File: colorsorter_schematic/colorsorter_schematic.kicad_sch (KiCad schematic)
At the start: 35 parts, among them SW2 SW_SPDT, U1 PIC24FJ64GA702-I/SO, U2 ESP8266-01_ESP-01

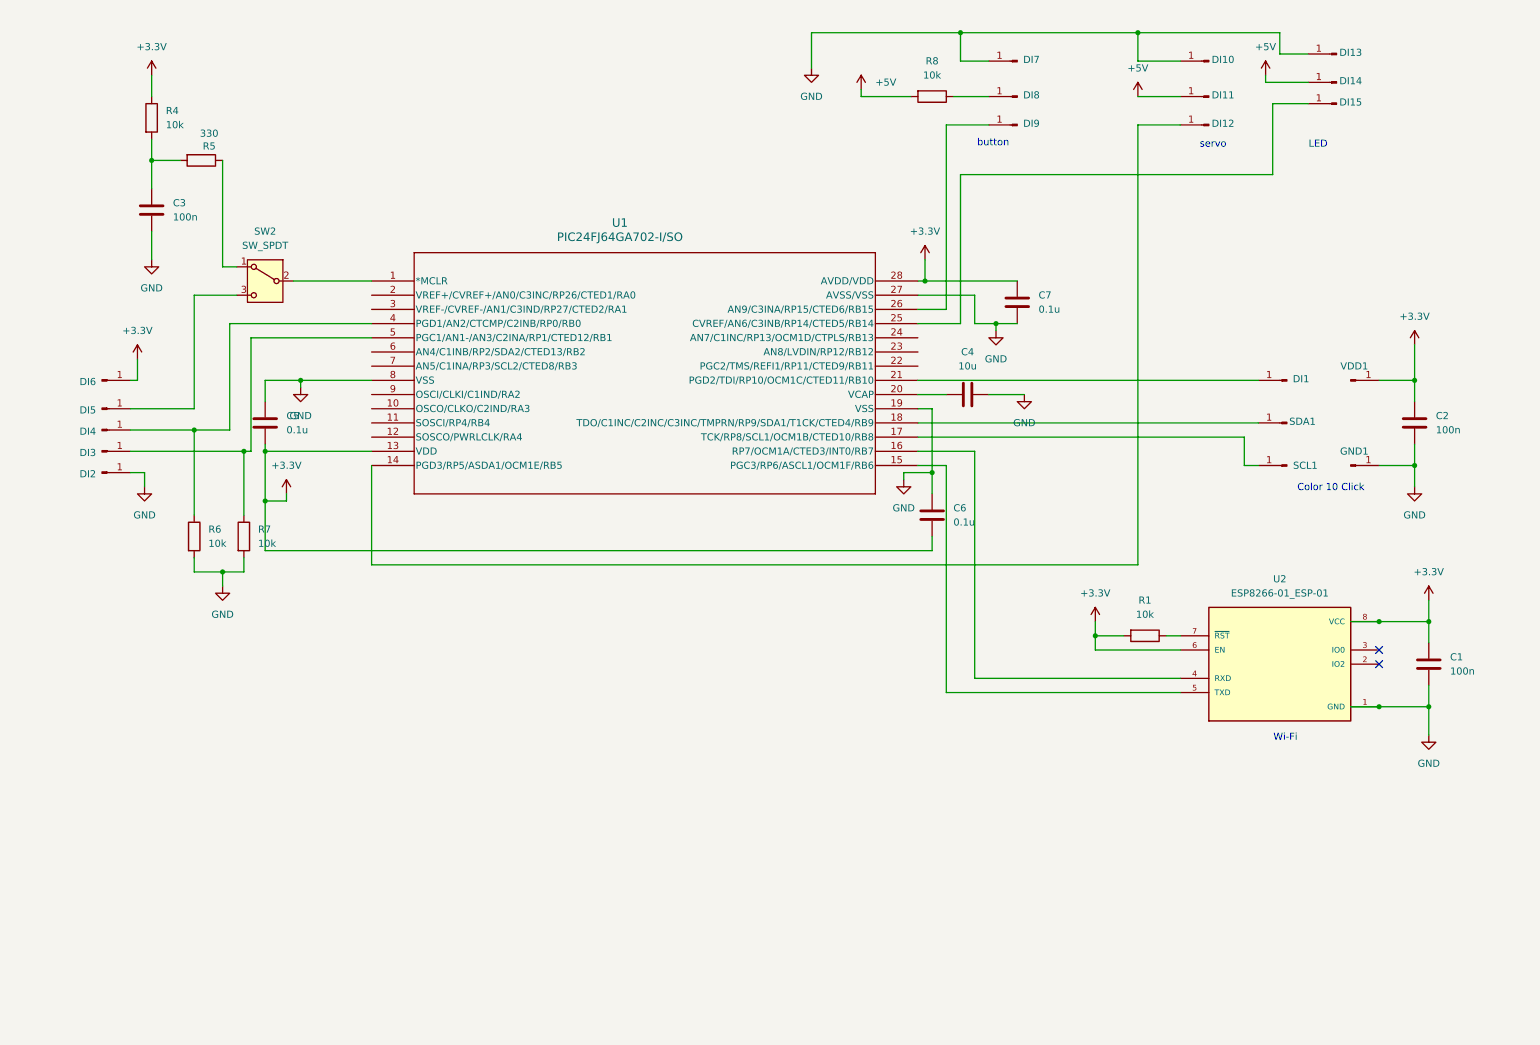
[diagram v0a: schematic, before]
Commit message: Added voltage regulator, oscillator and bulk capacitors.
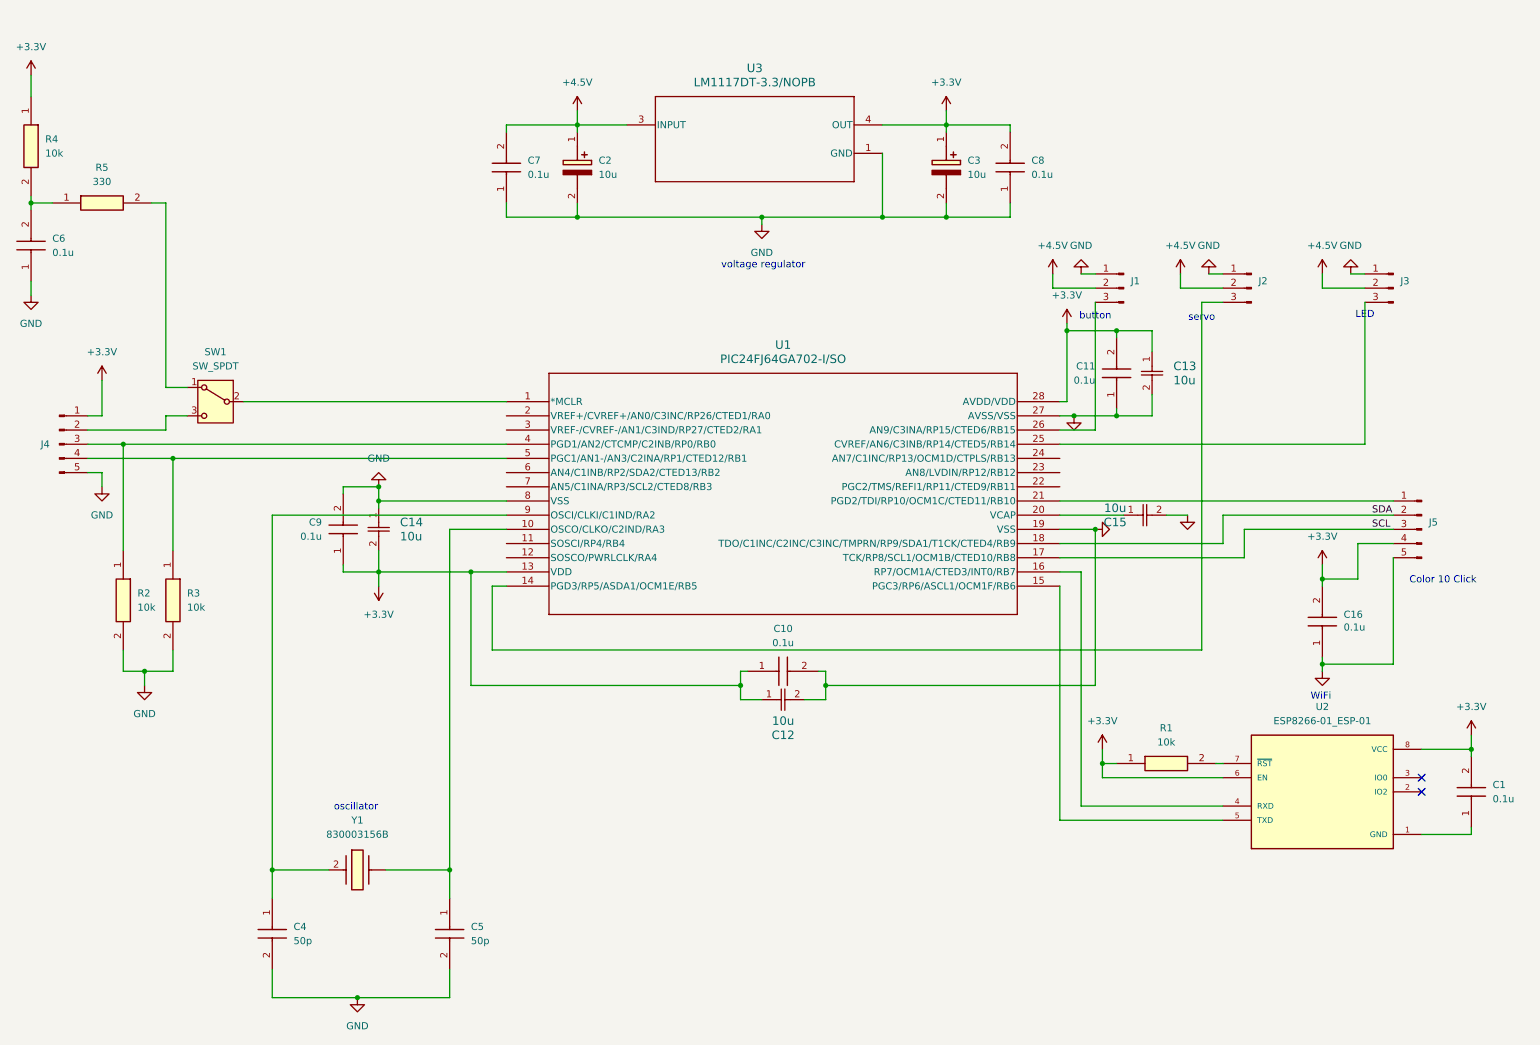
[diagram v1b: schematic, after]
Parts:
- removed C1, C2, C3: 100n, capacitor_smd:C_0805_2012Metric, symbol Device:C
- removed C4: 10u, symbol Device:C
- removed C5, C6, C7: 0.1u, symbol Device:C
- removed DI1, DI10, DI11, DI12, DI13, DI14, DI15, DI2, DI3, DI4, DI5, DI6, DI7, DI8, DI9, GND1, SCL1, SDA1, VDD1: Conn_01x01_Pin, symbol Connector:Conn_01x01_Pin
- removed R1, R4, R6, R7, R8: 10k, Resistor_SMD:R_0805_2012Metric, symbol Device:R
- removed R5: 330, Resistor_SMD:R_0805_2012Metric, symbol Device:R
- removed SW2: SW_SPDT, symbol Switch:SW_SPDT
- added C1, C10, C11, C16, C6, C7, C8, C9: 0.1u, CAPC2012X94N, symbol 0.1uF:KAM21BR71H104JT
- added C12, C13, C14, C15: 10u, CAP_2012_TDK, symbol 10uF:C2012X5R1C106K085AC
- added C2, C3: 10u, CAPPM6032X280N, symbol 10uFtantalum:293D106X9010C2TE3
- added C4, C5: 50p, CAPC2012X140N, symbol 50pF:08055A500FAT2A
- added J1, J2, J3: Conn_01x03_Pin, Connector_PinHeader_2.54mm:PinHeader_1x03_P2.54mm_Vertical, symbol Connector:Conn_01x03_Pin
- added J4, J5: Conn_01x05_Pin, Connector_PinHeader_2.54mm:PinHeader_1x05_P2.54mm_Vertical, symbol Connector:Conn_01x05_Pin
- added R1, R2, R3, R4: 10k, RESC2012X70N, symbol 10kohm:ERJ-S06F1002V
- added R5: 330, ERJP06D1000V, symbol 330ohm:ERJ-P06D3300V
- added SW1: SW_SPDT, symbol Switch:SW_SPDT
- added U3: LM1117DT-3.3/NOPB, NDP0003B, symbol voltageregulator:LM1117DT-3.3_NOPB
- added Y1: 830003156B, 830003156B, symbol crystaloscillator:830003156B
- U1: footprint SOIC28__SO28_MCH -> PIC24FJ64GA702-I-SO:SOIC28__SO28_MCH
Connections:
- net +3.3V: now also C1.2, C10.1, C11.2, C12.1, C13.1, C14.2, C16.2, C3.1 (+), C8.2, C9.1, J4.1 (Pin_1), J5.4 (Pin_4), R1.1, R4.1, U3.4 (OUT)
- net GND: now also C10.2, C11.1, C12.2, C13.2, C14.1, C15.2, C16.1, C2.2 (-), C3.2 (-), C4.2, C5.2, C6.1, C7.1, C8.1, C9.2, J1.1 (Pin_1), J2.1 (Pin_1), J3.1 (Pin_1), J4.5 (Pin_5), J5.5 (Pin_5), R2.2, R3.2, U3.1 (GND); no longer U2.1 (GND)
- net at U2.7 (~{RST}): now also R1.2
- net at U1.4 (PGD1/AN2/CTCMP/C2INB/RP0/RB0): now also J4.3 (Pin_3), R2.1
- net at U1.25 (CVREF/AN6/C3INB/RP14/CTED5/RB14): now also J3.3 (Pin_3)
- net at U1.1 (*MCLR): now also SW1.2 (B)
- net at U1.10 (OSCO/CLKO/C2IND/RA3): now also C5.1, Y1.
- net at U1.14 (PGD3/RP5/ASDA1/OCM1E/RB5): now also J2.3 (Pin_3)
- net SCL: now reaches U1.17 (TCK/RP8/SCL1/OCM1B/CTED10/RB8)
- net SCL: now also J5.3 (Pin_3)
- net SDA: now reaches U1.18 (TDO/C1INC/C2INC/C3INC/TMPRN/RP9/SDA1/T1CK/CTED4/RB9)
- net SDA: now also J5.2 (Pin_2)
- net at U1.20 (VCAP): now also C15.1
- net at U1.21 (PGD2/TDI/RP10/OCM1C/CTED11/RB10): now also J5.1 (Pin_1)
- net at U1.26 (AN9/C3INA/RP15/CTED6/RB15): now also J1.3 (Pin_3)
- net at U1.5 (PGC1/AN1-/AN3/C2INA/RP1/CTED12/RB1): now also J4.4 (Pin_4), R3.1
- net at U1.9 (OSCI/CLKI/C1IND/RA2): now also C4.1, Y1.2 (CRYSTAL_2)
- new net: C1.1, U2.1 (GND)
- new net: C6.2, R4.2, R5.1
- new net: R5.2, SW1.1 (A)
- new net: J4.2 (Pin_2), SW1.3 (C)
- new net +4.5V: C2.1 (+), C7.2, J1.2 (Pin_2), J2.2 (Pin_2), J3.2 (Pin_2), U3.3 (INPUT)
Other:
- note added: "WiFi"
- note added: "oscillator"
- note added: "voltage regulator"
- note removed: "Wi-Fi"

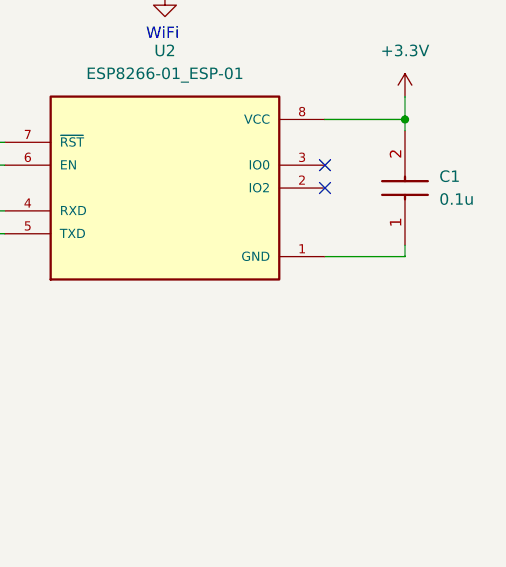
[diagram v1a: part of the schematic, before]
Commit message: Correction - added ground to WiFi module pin.
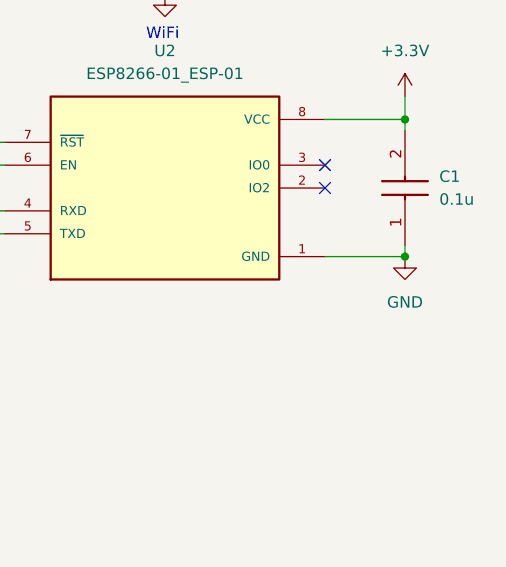
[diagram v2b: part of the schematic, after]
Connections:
- net GND: now also C1.1, U2.1 (GND)
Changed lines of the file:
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@@
 	)
 	(junction
+		(at 273.05 161.29)
+		(diameter 0)
+		(color 0 0 0 0)
+	)
+	(junction
 		(at 246.38 130.81)
 		(diameter 0)
@@
 					(unit 1)
 				)
+			)
+		)
+	)
+	(symbol
+		(lib_id "power:GND")
+		(at 273.05 161.29 0)
+		(unit 1)
+		(exclude_from_sim no)
+		(in_bom yes)
+		(on_board yes)
+		(dnp no)
+		(fields_autoplaced yes)
+		(property "Reference" "#PWR026"
+			(at 273.05 167.64 0)
+			(effects
+				(font
+					(size 1.27 1.27)
+				)
+				(hide yes)
+			)
+		)
+		(property "Value" "GND"
+			(at 273.05 166.37 0)
+			(effects
+				(font
+					(size 1.27 1.27)
+				)
+			)
+		)
+		(property "Footprint" ""
+			(at 273.05 161.29 0)
+			(effects
+				(font
+					(size 1.27 1.27)
+				)
+				(hide yes)
+			)
+		)
+		(property "Datasheet" ""
+			(at 273.05 161.29 0)
+			(effects
+				(font
+					(size 1.27 1.27)
+				)
+				(hide yes)
+			)
+		)
+		(property "Description" "Power symbol creates a global label with name \"GND\" , ground"
+			(at 273.05 161.29 0)
+			(effects
+				(font
+					(size 1.27 1.27)
+				)
+				(hide yes)
+			)
+		)
+		(pin "1"
+		)
+		(instances
+			(project "colorsorter_schematic"
+				(path "/f85b107f-670e-4885-9436-e3b5bb042aa6"
+					(reference "#PWR026")
+					(unit 1)
+				)

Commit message: Added additional pins header.
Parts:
- added J6, J7: Conn_01x03_Pin, Connector_PinHeader_2.54mm:PinHeader_1x03_P2.54mm_Vertical, symbol Connector:Conn_01x03_Pin
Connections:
- net at U1.11 (SOSCI/RP4/RB4): now also J7.3 (Pin_3)
- net at U1.22 (PGC2/TMS/REFI1/RP11/CTED9/RB11): now also J6.3 (Pin_3)
- net at U1.23 (AN8/LVDIN/RP12/RB12): now also J6.2 (Pin_2)
- net at U1.24 (AN7/C1INC/RP13/OCM1D/CTPLS/RB13): now also J6.1 (Pin_1)
- net at U1.6 (AN4/C1INB/RP2/SDA2/CTED13/RB2): now also J7.1 (Pin_1)
- net at U1.7 (AN5/C1INA/RP3/SCL2/CTED8/RB3): now also J7.2 (Pin_2)
- no-connect marks 2 -> 3
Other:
- note added: "additional pins"

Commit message: Dodavanje izmjena u semi i rutranje na pcb
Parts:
- added Power: Conn_01x02_Pin, symbol Connector:Conn_01x02_Pin
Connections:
- net +4.5V: now also Power.1 (Pin_1)
- net GND: now also Power.2 (Pin_2)
- no-connect marks 3 -> 5
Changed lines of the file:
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@@
 	)
 	(no_connect
+		(at 100.33 88.9)
+	)
+	(no_connect
+		(at 100.33 86.36)
+	)
+	(no_connect
 		(at 264.16 151.13)
 	)
@@
 	(wire
 		(pts
+			(xy 99.06 25.4) (xy 99.06 27.94)
+		)
+		(stroke
+			(width 0)
+			(type default)
+		)
+	)
+	(wire
+		(pts
 			(xy 259.08 130.81) (xy 246.38 130.81)
 		)
@@
 	(wire
 		(pts
+			(xy 99.06 20.32) (xy 99.06 22.86)
+		)
+		(stroke
+			(width 0)
+			(type default)
+		)
+	)
+	(wire
+		(pts
 			(xy 228.6 109.22) (xy 228.6 104.14)
 		)
@@
 	(wire
 		(pts
+			(xy 92.71 22.86) (xy 99.06 22.86)
+		)
+		(stroke
+			(width 0)
+			(type default)
+		)
+	)
+	(wire
+		(pts
 			(xy 90.17 96.52) (xy 90.17 38.1)
 		)
@@
 	(wire
 		(pts
+			(xy 92.71 25.4) (xy 99.06 25.4)
+		)
+		(stroke
+			(width 0)
+			(type default)
+		)
+	)
+	(wire
+		(pts
 			(xy 97.79 128.27) (xy 224.79 128.27)
 		)
@@
 	(symbol
 		(lib_id "power:GND")
+		(at 99.06 27.94 0)
+		(unit 1)
+		(exclude_from_sim no)
+		(in_bom yes)
+		(on_board yes)
+		(dnp no)
+		(fields_autoplaced yes)
+		(property "Reference" "#PWR028"
+			(at 99.06 34.29 0)
+			(effects
+				(font
+					(size 1.27 1.27)
+				)
+				(hide yes)
+			)
+		)
+		(property "Value" "GND"
+			(at 99.06 33.02 0)
+			(effects
+				(font
+					(size 1.27 1.27)
+				)
+			)
+		)
+		(property "Footprint" ""
+			(at 99.06 27.94 0)
+			(effects
+				(font
+					(size 1.27 1.27)
+				)
+				(hide yes)
+			)
+		)
+		(property "Datasheet" ""
+			(at 99.06 27.94 0)
+			(effects
+				(font
+					(size 1.27 1.27)
+				)
+				(hide yes)
+			)
+		)
+		(property "Description" "Power symbol creates a global label with name \"GND\" , ground"
+			(at 99.06 27.94 0)
+			(effects
+				(font
+					(size 1.27 1.27)
+				)
+				(hide yes)
+			)
+		)
+		(pin "1"
+		)
+		(instances
+			(project "colorsorter_schematic"
+				(path "/f85b107f-670e-4885-9436-e3b5bb042aa6"
+					(reference "#PWR028")
+					(unit 1)
+				)
+			)
+		)
+	)
+	(symbol
+		(lib_id "power:GND")
 		(at 226.06 60.96 0)
 		(mirror x)
@@
 	)
 	(symbol
+		(lib_id "Connector:Conn_01x02_Pin")
+		(at 87.63 22.86 0)
+		(unit 1)
+		(exclude_from_sim no)
+		(in_bom yes)
+		(on_board yes)
+		(dnp no)
+		(property "Reference" "Power"
+			(at 84.328 19.812 0)
+			(effects
+				(font
+					(size 1.27 1.27)
+				)
+			)
+		)
+		(property "Value" "Conn_01x02_Pin"
+			(at 86.614 28.448 0)
+			(effects
+				(font
+					(size 1.27 1.27)
+				)
+			)
+		)
+		(property "Footprint" ""
+			(at 87.63 22.86 0)
+			(effects
+				(font
+					(size 1.27 1.27)
+				)
+				(hide yes)
+			)
+		)
+		(property "Datasheet" "~"
+			(at 87.63 22.86 0)
+			(effects
+				(font
+					(size 1.27 1.27)
+				)
+				(hide yes)
+			)
+		)
+		(property "Description" "Generic connector, single row, 01x02, script generated"
+			(at 87.63 22.86 0)
+			(effects
+				(font
+					(size 1.27 1.27)
+				)
+				(hide yes)
+			)
+		)
+		(pin "2"
+		)
+		(pin "1"
+		)
+		(instances
+			(project ""
+				(path "/f85b107f-670e-4885-9436-e3b5bb042aa6"
+					(reference "Power")
+					(unit 1)
+				)
+			)
+		)
+	)
+	(symbol
 		(lib_id "10uFtantalum:293D106X9010C2TE3")
 		(at 113.03 35.56 270)
@@
 					(unit 1)
 				)
+			)
+		)
+	)
+	(symbol
+		(lib_id "power:VDD")
+		(at 99.06 20.32 0)
+		(unit 1)
+		(exclude_from_sim no)
+		(in_bom yes)
+		(on_board yes)
+		(dnp no)
+		(fields_autoplaced yes)
+		(property "Reference" "#PWR027"
+			(at 99.06 24.13 0)
+			(effects
+				(font
+					(size 1.27 1.27)
+				)
+				(hide yes)
+			)
+		)
+		(property "Value" "+4.5V"
+			(at 99.06 15.24 0)
+			(effects
+				(font
+					(size 1.27 1.27)
+				)
+			)
+		)
+		(property "Footprint" ""
+			(at 99.06 20.32 0)
+			(effects
+				(font
+					(size 1.27 1.27)
+				)
+				(hide yes)
+			)
+		)
+		(property "Datasheet" ""
+			(at 99.06 20.32 0)
+			(effects
+				(font
+					(size 1.27 1.27)
+				)
+				(hide yes)
+			)
+		)
+		(property "Description" "Power symbol creates a global label with name \"VDD\""
+			(at 99.06 20.32 0)
+			(effects
+				(font
+					(size 1.27 1.27)
+				)
+				(hide yes)
+			)
+		)
+		(pin "1"
+		)
+		(instances
+			(project "colorsorter_schematic"
+				(path "/f85b107f-670e-4885-9436-e3b5bb042aa6"
+					(reference "#PWR027")
+					(unit 1)
+				)

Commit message: Updated schematic.
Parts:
- U2: footprint ESP8266-01_ESP-01:XCVR_ESP8266-01_ESP-01 -> ESP8266-01_ESP-01:ESP8266-01_ESP-01
- renumbered Power to Power1
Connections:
- net +3.3V: no longer names the net of C1.2, C10.1, C11.2, C12.1, C13.1, C14.2, C16.2, C3.1 (+), C8.2, C9.1, J4.1 (Pin_1), J5.4 (Pin_4), R1.1, R4.1, U1.13 (VDD), U1.28 (AVDD/VDD), U2.6 (EN), U2.8 (VCC), U3.4 (OUT)
- net +4.5V: no longer names the net of C2.1 (+), C7.2, J1.2 (Pin_2), J2.2 (Pin_2), J3.2 (Pin_2), Power1.1 (Pin_1), U3.3 (INPUT)
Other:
- note added: "+3.3V"
- note added: "+4.5V"
- moved on the sheet: C6, Power1, R4, R5

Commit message: Updated schematic and pcb.
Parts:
- removed Power1: Conn_01x02_Pin, symbol Connector:Conn_01x02_Pin
- added J8: Conn_01x02_Pin, Connector_PinHeader_2.54mm:PinHeader_1x02_P2.54mm_Vertical, symbol Connector:Conn_01x02_Pin
- SW1: footprint (none) -> twostateswitch:SLW12768644AD
- U2: footprint ESP8266-01_ESP-01:ESP8266-01_ESP-01 -> wifi:wifi
- Y1: footprint 830003156B -> crystaloscillator:830003156B
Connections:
- net GND: now also J8.2 (Pin_2)
- net at C5.1, U1.10 (OSCO/CLKO/C2IND/RA3): now also Y1.1; no longer Y1.
- net at C2.1 (+), C7.2, J1.2 (Pin_2)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: now also J8.1 (Pin_1)
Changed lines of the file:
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@@
 			)
 		)
-		(property "Footprint" "830003156B"
+		(property "Footprint" "crystaloscillator:830003156B"
 			(at 77.47 263.83 0)
 			(effects
@@
 			)
 		)
-		(pin ""
+		(pin "1"
 		)
 		(pin "2"
@@
 	)
 	(symbol
-		(lib_id "Connector:Conn_01x02_Pin")
-		(at 87.63 20.32 0)
-		(unit 1)
-		(exclude_from_sim no)
-		(in_bom yes)
-		(on_board yes)
-		(dnp no)
-		(property "Reference" "Power1"
-			(at 83.566 20.32 0)
-			(effects
-				(font
-					(size 1.27 1.27)
-				)
-			)
-		)
-		(property "Value" "Conn_01x02_Pin"
-			(at 86.614 25.908 0)
-			(effects
-				(font
-					(size 1.27 1.27)
-				)
-			)
-		)
-		(property "Footprint" ""
-			(at 87.63 20.32 0)
-			(effects
-				(font
-					(size 1.27 1.27)
-				)
-				(hide yes)
-			)
-		)
-		(property "Datasheet" "~"
-			(at 87.63 20.32 0)
-			(effects
-				(font
-					(size 1.27 1.27)
-				)
-				(hide yes)
-			)
-		)
-		(property "Description" "Generic connector, single row, 01x02, script generated"
-			(at 87.63 20.32 0)
-			(effects
-				(font
-					(size 1.27 1.27)
-				)
-				(hide yes)
-			)
-		)
-		(pin "2"
-		)
-		(pin "1"
-		)
-		(instances
-			(project ""
-				(path "/f85b107f-670e-4885-9436-e3b5bb042aa6"
-					(reference "Power1")
-					(unit 1)
-				)
-			)
-		)
-	)
-	(symbol
 		(lib_id "10uFtantalum:293D106X9010C2TE3")
 		(at 113.03 35.56 270)
@@
 			)
 		)
-		(property "Footprint" "ESP8266-01_ESP-01:ESP8266-01_ESP-01"
+		(property "Footprint" "wifi:wifi"
 			(at 246.38 153.67 0)
 			(effects
@@
 			)
 		)
-		(property "Footprint" ""
+		(property "Footprint" "twostateswitch:SLW12768644AD"
 			(at 48.26 83.82 0)
 			(effects
@@
 					(unit 1)
 				)
+			)
+		)
+	)
+	(symbol
+		(lib_id "Connector:Conn_01x02_Pin")
+		(at 87.63 20.32 0)
+		(unit 1)
+		(exclude_from_sim no)
+		(in_bom yes)
+		(on_board yes)
+		(dnp no)
+		(fields_autoplaced yes)
+		(property "Reference" "J8"
+			(at 88.265 15.24 0)
+			(effects
+				(font
+					(size 1.27 1.27)
+				)
+			)
+		)
+		(property "Value" "Conn_01x02_Pin"
+			(at 88.265 17.78 0)
+			(effects
+				(font
+					(size 1.27 1.27)
+				)
+			)
+		)
+		(property "Footprint" "Connector_PinHeader_2.54mm:PinHeader_1x02_P2.54mm_Vertical"
+			(at 87.63 20.32 0)
+			(effects
+				(font
+					(size 1.27 1.27)
+				)
+				(hide yes)
+			)
+		)
+		(property "Datasheet" "~"
+			(at 87.63 20.32 0)
+			(effects
+				(font
+					(size 1.27 1.27)
+				)
+				(hide yes)
+			)
+		)
+		(property "Description" "Generic connector, single row, 01x02, script generated"
+			(at 87.63 20.32 0)
+			(effects
+				(font
+					(size 1.27 1.27)
+				)
+				(hide yes)
+			)
+		)
+		(pin "2"
+		)
+		(pin "1"
+		)
+		(instances
+			(project ""
+				(path "/f85b107f-670e-4885-9436-e3b5bb042aa6"
+					(reference "J8")
+					(unit 1)
+				)
